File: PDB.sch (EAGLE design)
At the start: 76 parts, among them IC1 LM555N

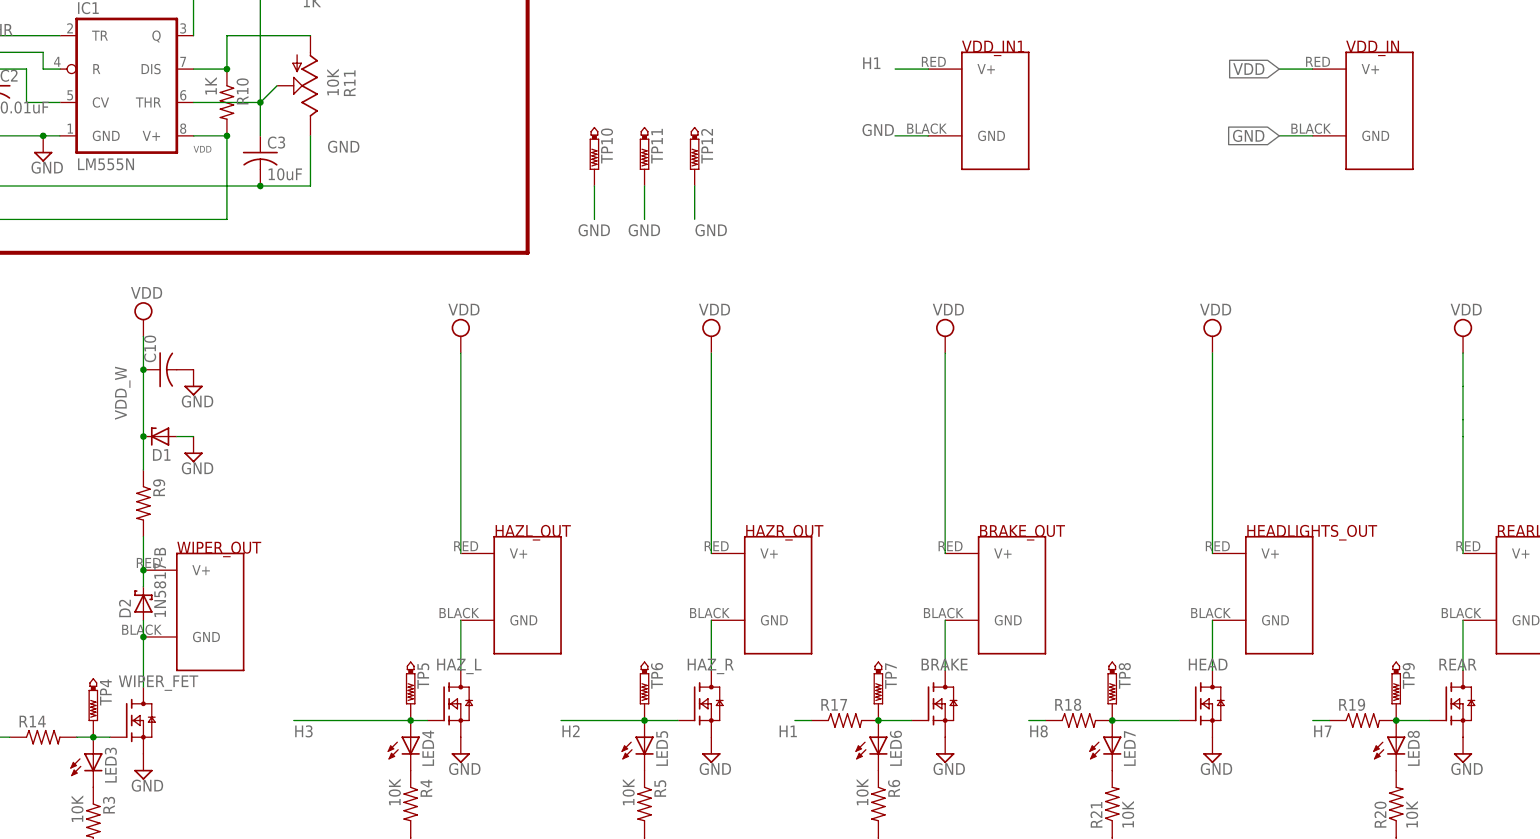
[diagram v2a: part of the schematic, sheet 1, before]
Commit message: changed GND of brake sensor to VDD
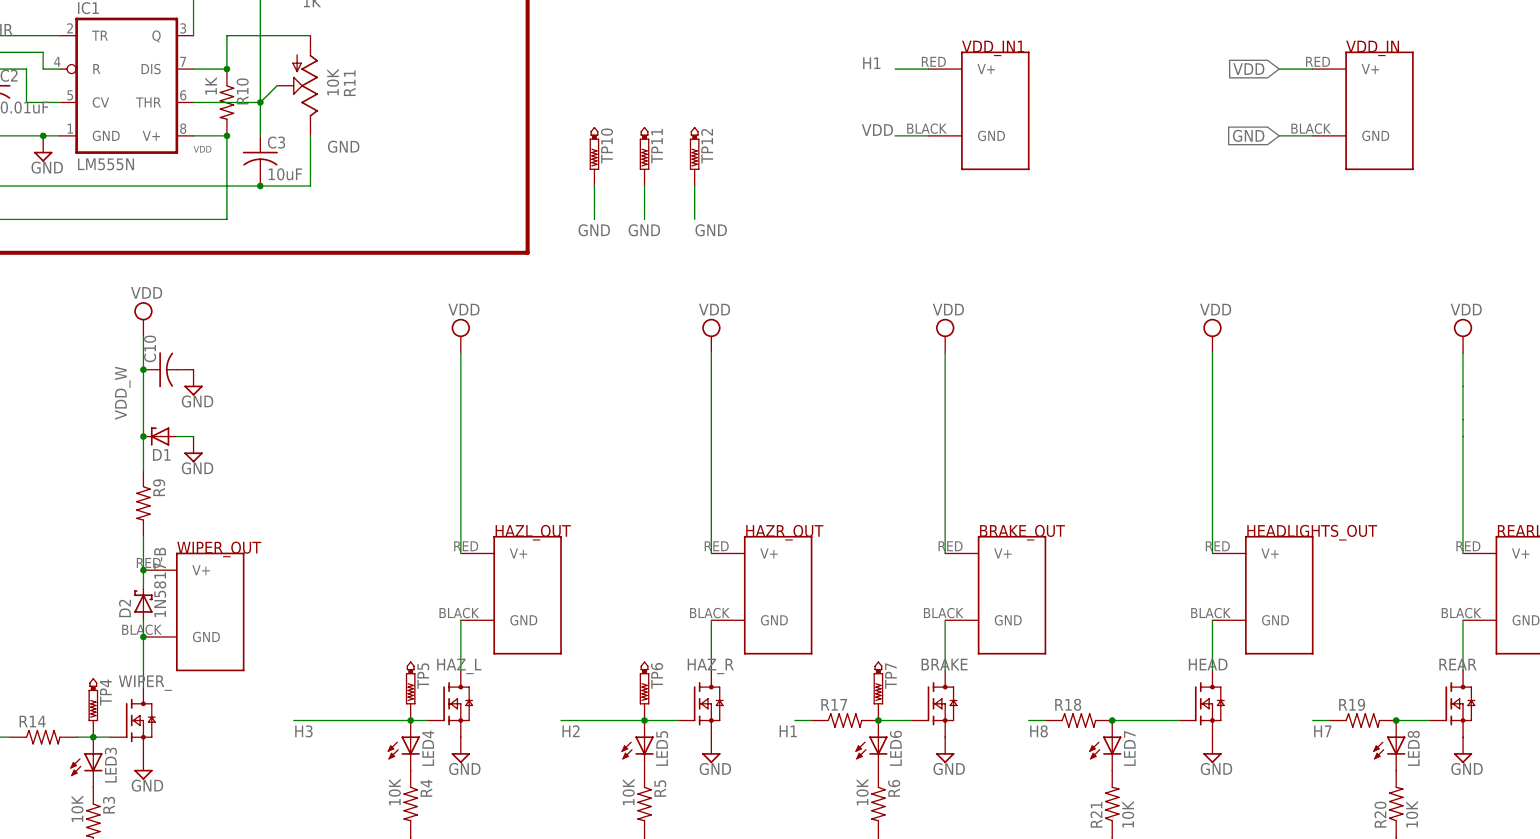
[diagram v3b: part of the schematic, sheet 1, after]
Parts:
- removed TP8, TP9: PTR1B2,54, testpad:PTR1B2,54
- renumbered WIPER_FET to WIPER_
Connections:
- net GND: no longer VDD_IN1.GND
- net N$14: no longer TP8.TP
- net N$15: no longer TP9.TP
- net VDD: now also VDD_IN1.GND
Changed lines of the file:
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@@
 <part name="SUPPLY11" library="supply2" library_urn="urn:adsk.eagle:library:372" deviceset="VDD" device=""/>
 <part name="SUPPLY28" library="supply2" library_urn="urn:adsk.eagle:library:372" deviceset="GND" device=""/>
-<part name="WIPER_FET" library="nxp_60" deviceset="PSMN" device="YS" technology="039-100"/>
+<part name="WIPER_" library="nxp_60" deviceset="PSMN" device="YS" technology="039-100"/>
 <part name="R9" library="rcl" library_urn="urn:adsk.eagle:library:334" deviceset="R-US_" device="R0805" package3d_urn="urn:adsk.eagle:package:23553/2"/>
 <part name="C10" library="rcl" library_urn="urn:adsk.eagle:library:334" deviceset="C-US" device="C0805" package3d_urn="urn:adsk.eagle:package:23617/2"/>
@@
 <part name="TP6" library="testpad" library_urn="urn:adsk.eagle:library:385" deviceset="PTR1" device="B2,54" package3d_urn="urn:adsk.eagle:package:27948/1"/>
 <part name="TP7" library="testpad" library_urn="urn:adsk.eagle:library:385" deviceset="PTR1" device="B2,54" package3d_urn="urn:adsk.eagle:package:27948/1"/>
-<part name="TP8" library="testpad" library_urn="urn:adsk.eagle:library:385" deviceset="PTR1" device="B2,54" package3d_urn="urn:adsk.eagle:package:27948/1"/>
-<part name="TP9" library="testpad" library_urn="urn:adsk.eagle:library:385" deviceset="PTR1" device="B2,54" package3d_urn="urn:adsk.eagle:package:27948/1"/>
 <part name="TP10" library="testpad" library_urn="urn:adsk.eagle:library:385" deviceset="PTR1" device="PAD1-13Y" package3d_urn="urn:adsk.eagle:package:27947/1"/>
 <part name="TP11" library="testpad" library_urn="urn:adsk.eagle:library:385" deviceset="PTR1" device="PAD1-13Y" package3d_urn="urn:adsk.eagle:package:27947/1"/>
@@
 <attribute name="VALUE" x="-29.845" y="-3.175" size="1.778" layer="96"/>
 </instance>
-<instance part="WIPER_FET" gate="G$1" x="12.7" y="5.08" smashed="yes">
+<instance part="WIPER_" gate="G$1" x="12.7" y="5.08" smashed="yes">
 <attribute name="NAME" x="11.43" y="10.16" size="1.778" layer="95" font="vector"/>
 </instance>
@@
 <instance part="TP6" gate="G$1" x="91.44" y="7.62" rot="R180"/>
 <instance part="TP7" gate="G$1" x="127" y="7.62" rot="R180"/>
-<instance part="TP8" gate="G$1" x="162.56" y="7.62" rot="R180"/>
-<instance part="TP9" gate="G$1" x="205.74" y="7.62" rot="R180"/>
 <instance part="TP10" gate="G$1" x="83.82" y="88.9" rot="R180"/>
 <instance part="TP11" gate="G$1" x="91.44" y="88.9" rot="R180"/>
@@
 </segment>
 <segment>
-<pinref part="WIPER_FET" gate="G$1" pin="S"/>
+<pinref part="WIPER_" gate="G$1" pin="S"/>
 <pinref part="SUPPLY30" gate="GND" pin="GND"/>
 </segment>
@@
 <pinref part="SUPPLY22" gate="GND" pin="GND"/>
 <pinref part="R20" gate="G$1" pin="1"/>
-</segment>
-<segment>
-<pinref part="VDD_IN1" gate="G$1" pin="GND"/>
-<wire x1="134.62" y1="93.98" x2="129.54" y2="93.98" width="0.1524" layer="91"/>
-<label x="124.46" y="93.98" size="1.778" layer="95"/>
 </segment>
 <segment>
@@
 <junction x="-12.7" y="86.36"/>
 </segment>
+<segment>
+<pinref part="VDD_IN1" gate="G$1" pin="GND"/>
+<wire x1="134.62" y1="93.98" x2="129.54" y2="93.98" width="0.1524" layer="91"/>
+<label x="124.46" y="93.98" size="1.778" layer="95"/>
+</segment>
 </net>
 <net name="N$8" class="0">
@@
 <net name="N$19" class="0">
 <segment>
-<pinref part="WIPER_FET" gate="G$1" pin="D"/>
+<pinref part="WIPER_" gate="G$1" pin="D"/>
 <wire x1="15.24" y1="10.16" x2="15.24" y2="17.78" width="0.1524" layer="91"/>
 <pinref part="WIPER_OUT" gate="G$1" pin="GND"/>
@@
 <wire x1="172.72" y1="5.08" x2="162.56" y2="5.08" width="0.1524" layer="91"/>
 <junction x="162.56" y="5.08"/>
-<pinref part="TP8" gate="G$1" pin="TP"/>
 </segment>
 </net>
@@
 <wire x1="210.82" y1="5.08" x2="205.74" y2="5.08" width="0.1524" layer="91"/>
 <junction x="205.74" y="5.08"/>
-<pinref part="TP9" gate="G$1" pin="TP"/>
 </segment>
 </net>
 <net name="N$22" class="0">
 <segment>
-<pinref part="WIPER_FET" gate="G$1" pin="G"/>
+<pinref part="WIPER_" gate="G$1" pin="G"/>
 <pinref part="R14" gate="G$1" pin="2"/>
 <wire x1="10.16" y1="2.54" x2="7.62" y2="2.54" width="0.1524" layer="91"/>

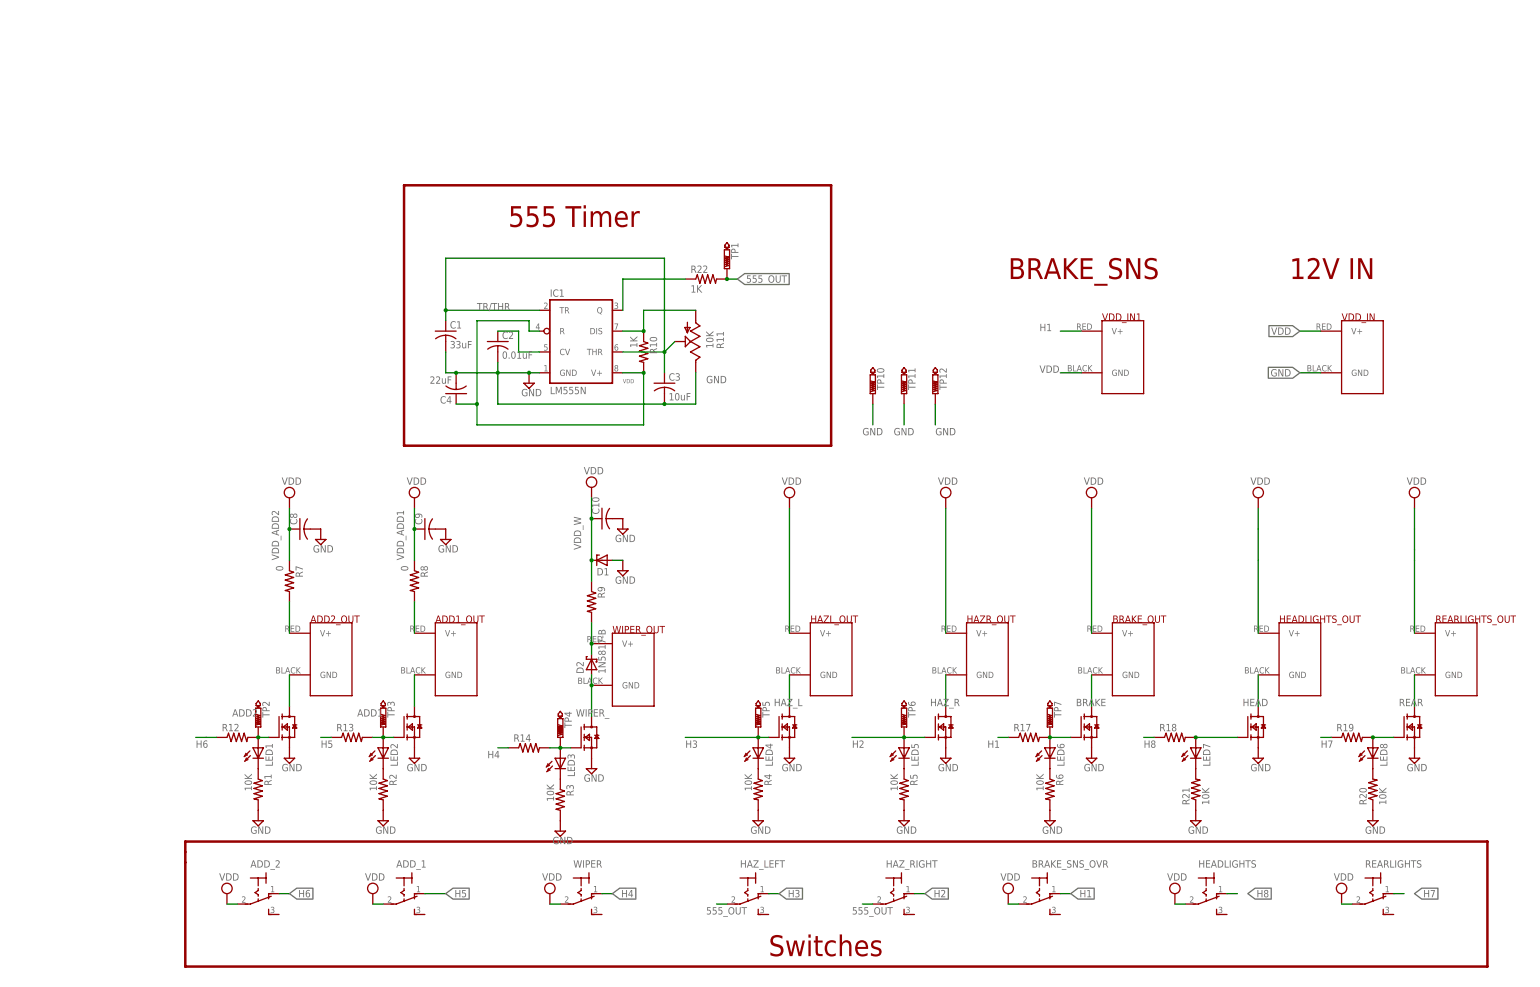
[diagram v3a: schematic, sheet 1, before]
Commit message: thickened traces
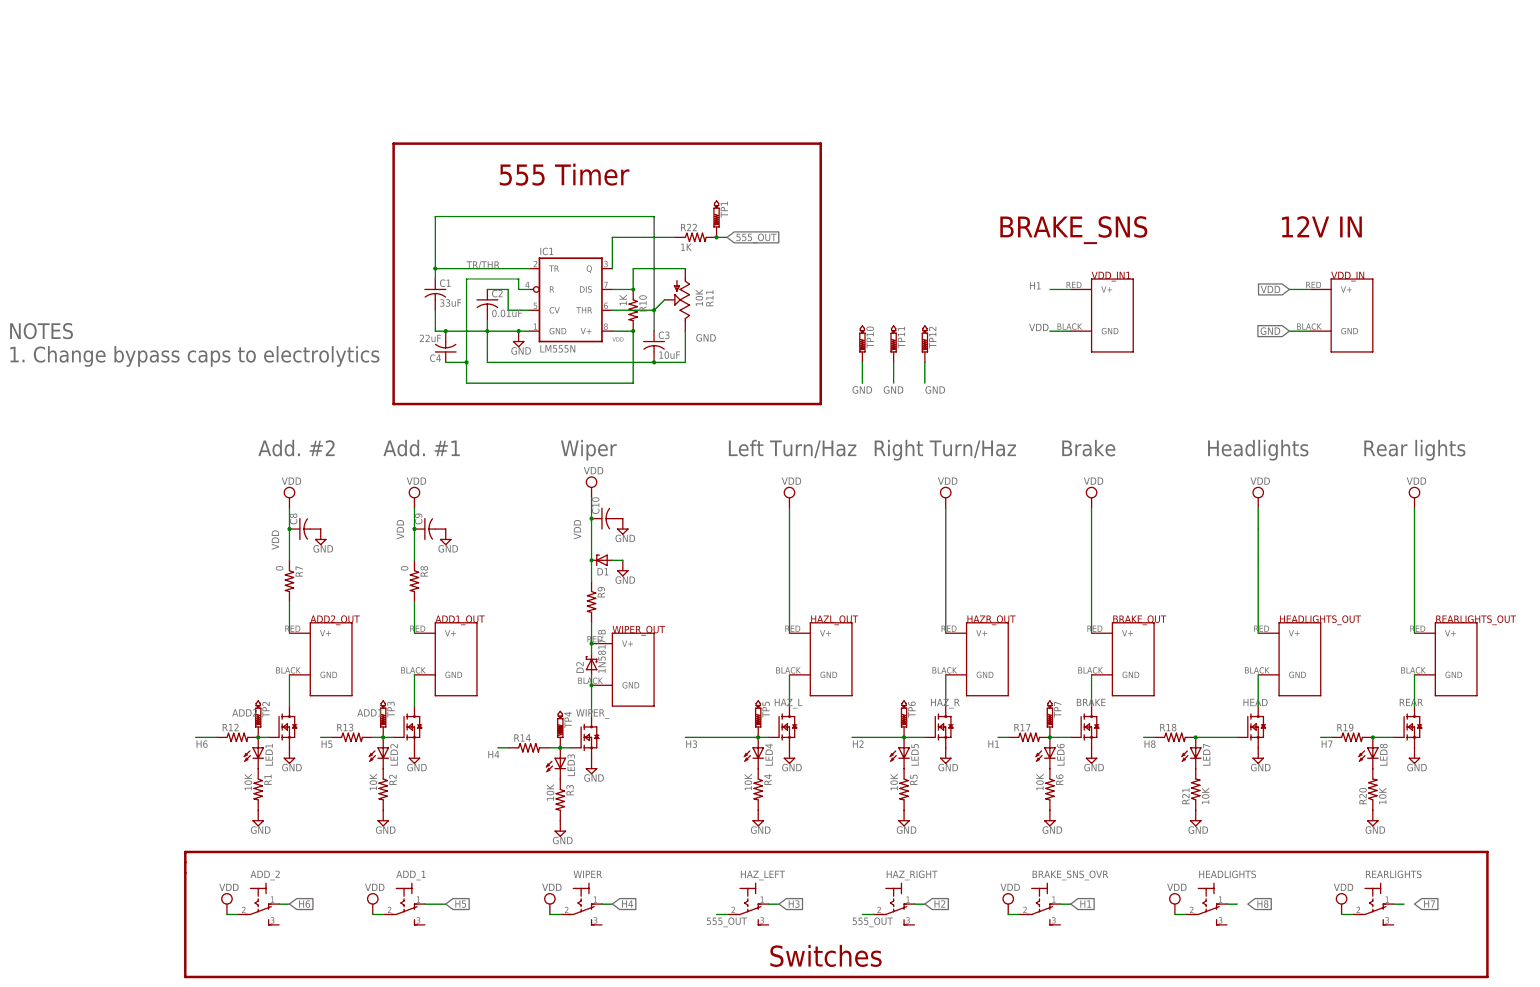
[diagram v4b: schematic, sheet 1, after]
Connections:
- removed net VDD_ADD1: C9.1, R8.1
- removed net VDD_ADD2: C8.1, R7.1
- removed net VDD_W: C10.1, D1.C, R9.1
- net VDD: now also C10.1, C8.1, C9.1, D1.C, R7.1, R8.1, R9.1
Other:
- note added: "Add. #1"
- note added: "Add. #2"
- note added: "Brake"
- note added: "Headlights"
- note added: "Left Turn/Haz"
- note added: "NOTES 1. Change bypass caps to electrolytics"
- note added: "Rear lights"
- note added: "Right Turn/Haz"
- note added: "Wiper"
- moved on the sheet: ADD_1, ADD_2, BRAKE_SNS_OVR, C1, C2, C3, C4, HAZ_LEFT, HAZ_RIGHT, HEADLIGHTS, IC1, R10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

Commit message: changed switches for Add 1, 2.
made compatible with JST connector
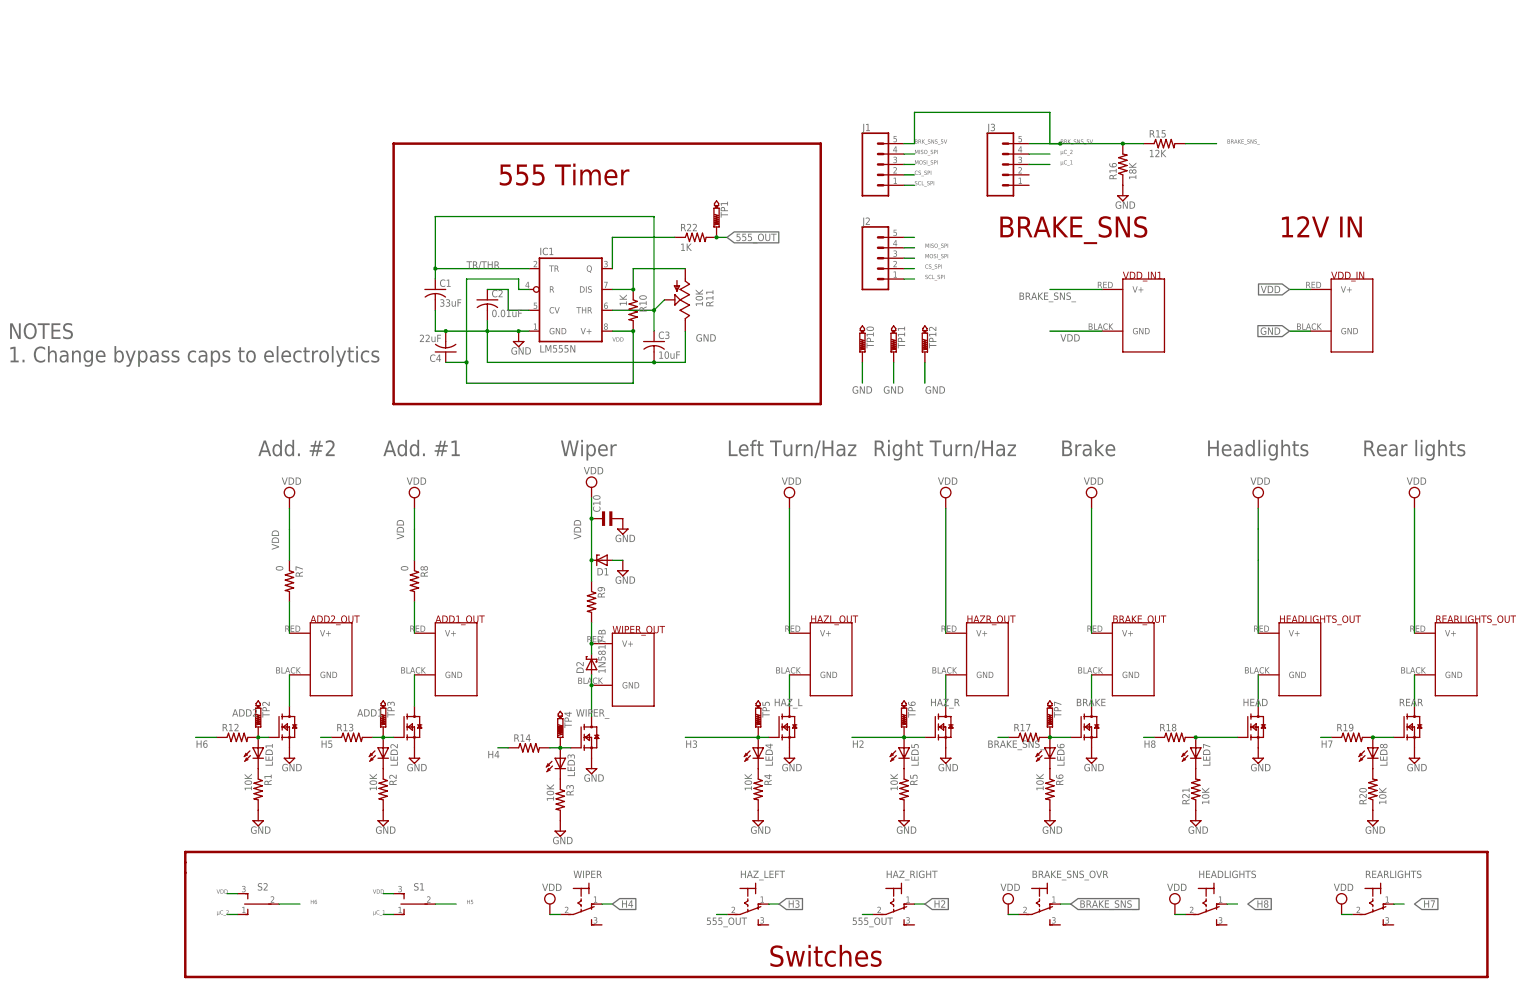
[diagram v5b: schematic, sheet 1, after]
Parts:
- removed ADD_1, ADD_2: (no value), switch:M9040P
- removed C8, C9: (no value), rcl:C-USC0805
- added J1, J2, J3: (no value), SparkFun-Connectors:CONN_05JST
- added R15: 12K, resistor:R-US_R2512
- added R16: 18K, resistor:R-US_R2512
- added S1, S2: TL39PO, switch:TL39PO
- C10: device rcl:C-USC0805 -> resistor:EL-BI25-10AXIAL
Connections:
- removed net H1: BRAKE_SNS_OVR.O, R17.1, VDD_IN1.V+
- new net BRAKE_SNS_: BRAKE_SNS_OVR.O, R15.2, R17.1, VDD_IN1.V+
- new net BRK_SNS_5V: J1.5, J3.5, R15.1, R16.2
- new net CS_SPI: J1.2, J2.2
- new net MISO_SPI: J1.4, J2.4
- new net MOSI_SPI: J1.3, J2.3
- new net N$12: J2.5
- new net SCL_SPI: J1.1, J2.1
- new net µC_1: J3.3, S1.O
- new net µC_2: J3.4, S2.O
- net GND: now also R16.1; no longer C8.2, C9.2
- net H5: now also S1.P; no longer ADD_1.O
- net H6: now also S2.P; no longer ADD_2.O
- net VDD: now also S1.S, S2.S; no longer ADD_1.P, ADD_2.P, C8.1, C9.1
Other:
- moved on the sheet: VDD_IN1
